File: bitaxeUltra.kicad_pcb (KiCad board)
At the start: 4 copper layers, 56.5 x 99.8 mm, 137 parts, among them J1 54-00164, J2 Conn_01x02, J3 Conn_01x05, J4 Conn_01x04, J5 TC2030-IDC, J7 Conn_01x02, J8 USB_C_Receptacle_USB2.0, J9 Conn_01x04, Q1 CSD17311Q5, Q2 CSD17311Q5, Q4 2N7002K, SW1 GT-TC029B-H025-L1N, SW2 GT-TC029B-H025-L1N, U1 25MHz, U10 DS4432U+, U11 RT9080-33GJ5, U12 ESP32-S3-WROOM-1, U14 BM1366_mode1, U2 TXB0104RGYR, U5 MCP1824T-1802E, U6 MCP1824T-0802E, U7 EMC2101, U8 INA260, U9 TPS40305, Y1 32.768kHz

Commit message: Init commit to TCH-204 Black edition with LED lights
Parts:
- removed TP23: TestPoint, TestPoint:TestPoint_Pad_D1.5mm
- added G***: LOGO, LOGO, B.Cu at (107.2, 52.8)
- added LED**: LED-RF-Controller, bitaxe:LED-RF-Controller, F.Cu at (103.1, 53.8)
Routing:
- net GND: track 148.3 -> 173.2 mm
- net /5V: track 217.6 -> 231.1 mm
- net /SDA: track 128.0 -> 126.8 mm

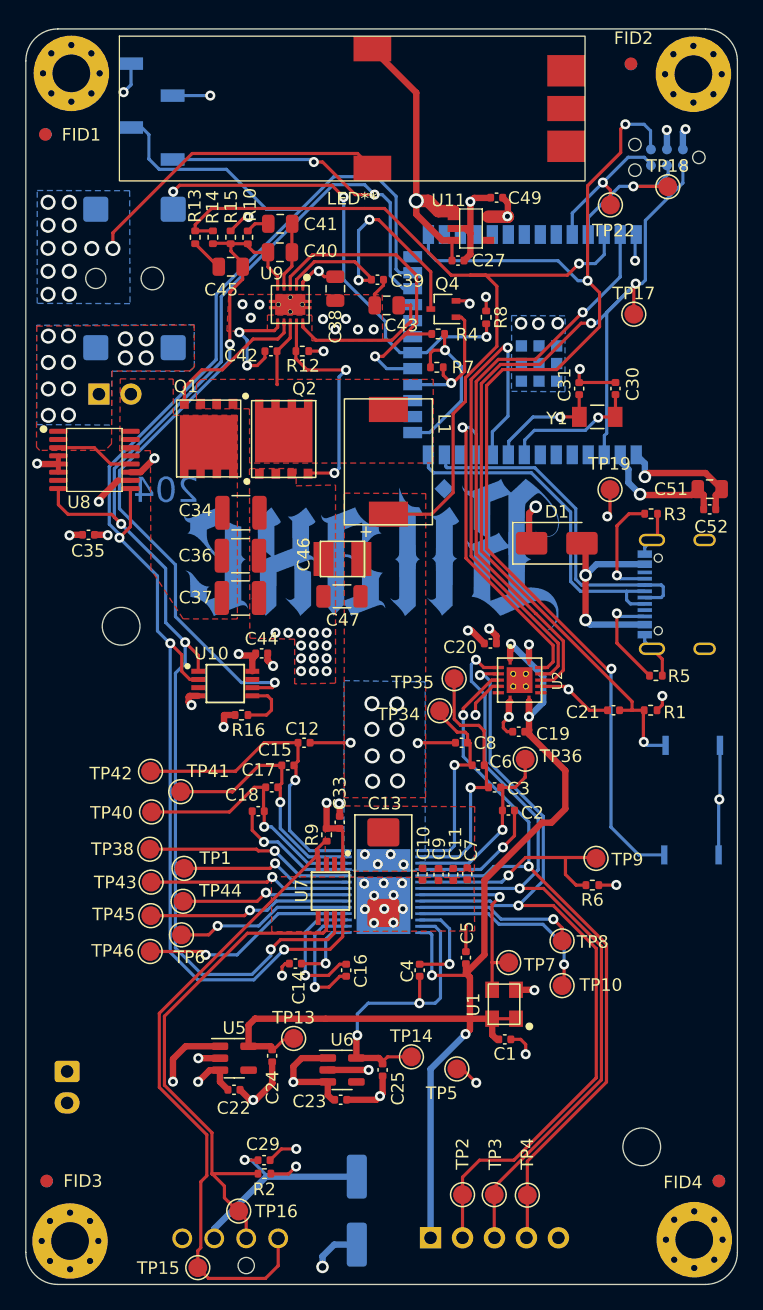
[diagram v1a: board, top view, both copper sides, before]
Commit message: Finish LED layout. Can pass to factory for prototype test
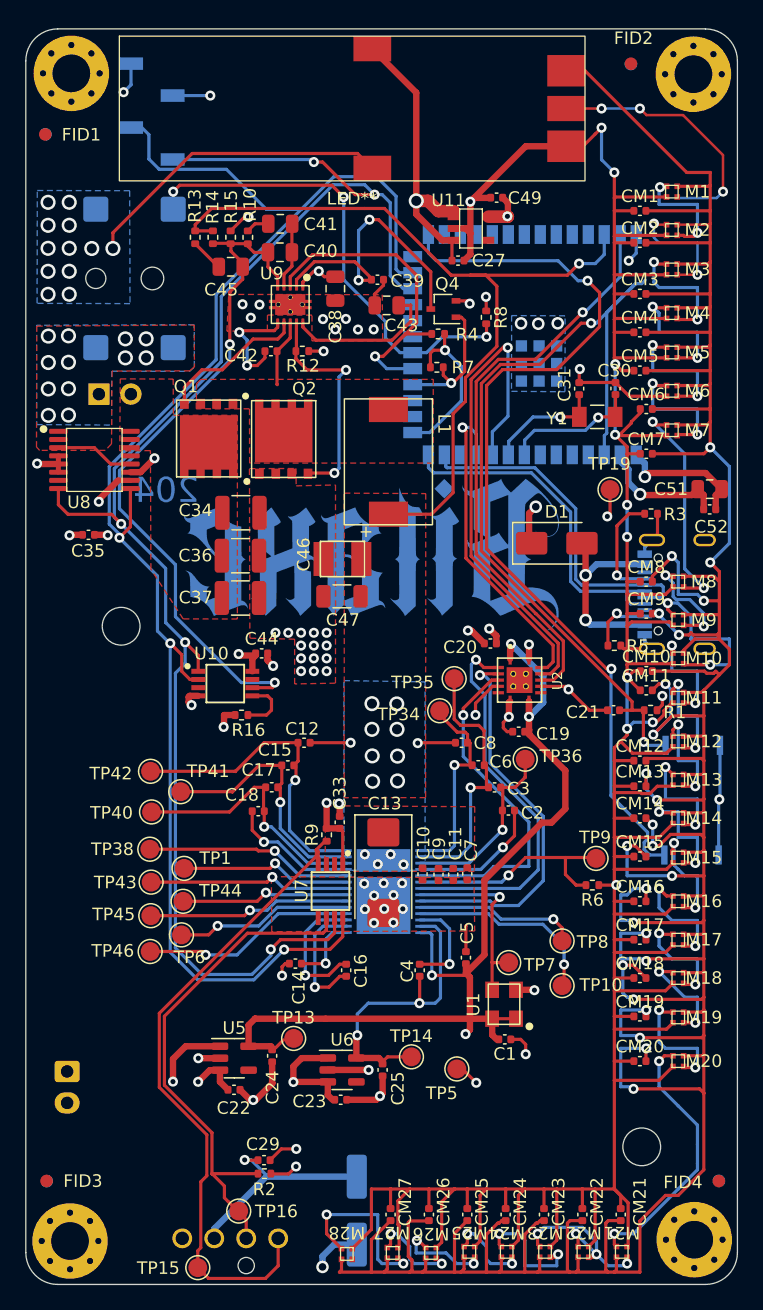
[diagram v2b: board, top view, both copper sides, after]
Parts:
- removed J3: Conn_01x05, Connector_PinHeader_2.54mm:PinHeader_1x05_P2.54mm_Vertical
- removed J5: TC2030-IDC, bitaxe:Tag-Connect_TC2030-IDC-NL_2x03_P1.27mm_Vertical
- removed TP17, TP18, TP2, TP22, TP3, TP4: TestPoint, TestPoint:TestPoint_Pad_D1.5mm
- added CM1: 0.1uF, Capacitor_SMD:C_0402_1005Metric, F.Cu at (126.0, 62.0)
- added CM10: 0.1uF, Capacitor_SMD:C_0402_1005Metric, F.Cu at (126.5, 98.6)
- added CM11: 0.1uF, Capacitor_SMD:C_0402_1005Metric, F.Cu at (126.5, 100.1)
- added CM12: 0.1uF, Capacitor_SMD:C_0402_1005Metric, F.Cu at (126.0, 105.7)
- added CM13: 0.1uF, Capacitor_SMD:C_0402_1005Metric, F.Cu at (126.0, 107.7)
- added CM14: 0.1uF, Capacitor_SMD:C_0402_1005Metric, F.Cu at (126.0, 110.2)
- added CM15: 0.1uF, Capacitor_SMD:C_0402_1005Metric, F.Cu at (126.0, 113.3)
- added CM16: 0.1uF, Capacitor_SMD:C_0402_1005Metric, F.Cu at (126.0, 116.8)
- added CM17: 0.1uF, Capacitor_SMD:C_0402_1005Metric, F.Cu at (126.0, 119.9)
- added CM18: 0.1uF, Capacitor_SMD:C_0402_1005Metric, F.Cu at (126.0, 122.9)
- added CM19: 0.1uF, Capacitor_SMD:C_0402_1005Metric, F.Cu at (126.0, 126.0)
- added CM2: 0.1uF, Capacitor_SMD:C_0402_1005Metric, F.Cu at (126.0, 64.5)
- added CM20: 0.1uF, Capacitor_SMD:C_0402_1005Metric, F.Cu at (126.0, 129.5)
- added CM21: 0.1uF, Capacitor_SMD:C_0402_1005Metric, F.Cu at (124.5, 141.7)
- added CM22: 0.1uF, Capacitor_SMD:C_0402_1005Metric, F.Cu at (121.4, 141.7)
- added CM23: 0.1uF, Capacitor_SMD:C_0402_1005Metric, F.Cu at (118.4, 141.7)
- added CM24: 0.1uF, Capacitor_SMD:C_0402_1005Metric, F.Cu at (115.3, 141.7)
- added CM25: 0.1uF, Capacitor_SMD:C_0402_1005Metric, F.Cu at (112.3, 141.7)
- added CM26: 0.1uF, Capacitor_SMD:C_0402_1005Metric, F.Cu at (109.2, 141.7)
- added CM27: 0.1uF, Capacitor_SMD:C_0402_1005Metric, F.Cu at (106.2, 141.7)
- added CM3: 0.1uF, Capacitor_SMD:C_0402_1005Metric, F.Cu at (126.0, 68.6)
- added CM4: 0.1uF, Capacitor_SMD:C_0402_1005Metric, F.Cu at (126.0, 71.6)
- added CM5: 0.1uF, Capacitor_SMD:C_0402_1005Metric, F.Cu at (126.0, 74.7)
- added CM6: 0.1uF, Capacitor_SMD:C_0402_1005Metric, F.Cu at (126.5, 77.7)
- added CM7: 0.1uF, Capacitor_SMD:C_0402_1005Metric, F.Cu at (126.5, 81.3)
- added CM8: 0.1uF, Capacitor_SMD:C_0402_1005Metric, F.Cu at (126.5, 91.4)
- added CM9: 0.1uF, Capacitor_SMD:C_0402_1005Metric, F.Cu at (126.5, 94.0)
- added M1: XL-1010RGBC, bitaxe:XL-1010RGBC, F.Cu at (128.5, 60.5)
- added M10: XL-1010RGBC, bitaxe:XL-1010RGBC, F.Cu at (129.0, 97.5)
- added M11: XL-1010RGBC, bitaxe:XL-1010RGBC, F.Cu at (129.0, 100.7)
- added M12: XL-1010RGBC, bitaxe:XL-1010RGBC, F.Cu at (129.0, 104.1)
- added M13: XL-1010RGBC, bitaxe:XL-1010RGBC, F.Cu at (129.0, 107.2)
- added M14: XL-1010RGBC, bitaxe:XL-1010RGBC, F.Cu at (129.0, 110.2)
- added M15: XL-1010RGBC, bitaxe:XL-1010RGBC, F.Cu at (129.0, 113.4)
- added M16: XL-1010RGBC, bitaxe:XL-1010RGBC, F.Cu at (129.0, 116.8)
- added M17: XL-1010RGBC, bitaxe:XL-1010RGBC, F.Cu at (129.0, 119.9)
- added M18: XL-1010RGBC, bitaxe:XL-1010RGBC, F.Cu at (129.0, 122.9)
- added M19: XL-1010RGBC, bitaxe:XL-1010RGBC, F.Cu at (129.0, 126.1)
- added M2: XL-1010RGBC, bitaxe:XL-1010RGBC, F.Cu at (128.5, 63.5)
- added M20: XL-1010RGBC, bitaxe:XL-1010RGBC, F.Cu at (129.0, 129.5)
- added M21: XL-1010RGBC, bitaxe:XL-1010RGBC, F.Cu at (124.5, 144.7)
- added M22: XL-1010RGBC, bitaxe:XL-1010RGBC, F.Cu at (121.5, 144.7)
- added M23: XL-1010RGBC, bitaxe:XL-1010RGBC, F.Cu at (118.4, 144.7)
- added M24: XL-1010RGBC, bitaxe:XL-1010RGBC, F.Cu at (115.4, 144.7)
- added M25: XL-1010RGBC, bitaxe:XL-1010RGBC, F.Cu at (112.4, 144.7)
- added M26: XL-1010RGBC, bitaxe:XL-1010RGBC, F.Cu at (109.4, 144.8)
- added M27: XL-1010RGBC, bitaxe:XL-1010RGBC, F.Cu at (106.3, 144.8)
- added M28: XL-1010RGBC, bitaxe:XL-1010RGBC, F.Cu at (102.7, 144.9)
- added M3: XL-1010RGBC, bitaxe:XL-1010RGBC, F.Cu at (128.5, 66.6)
- added M4: XL-1010RGBC, bitaxe:XL-1010RGBC, F.Cu at (128.5, 70.1)
- added M5: XL-1010RGBC, bitaxe:XL-1010RGBC, F.Cu at (128.5, 73.2)
- added M6: XL-1010RGBC, bitaxe:XL-1010RGBC, F.Cu at (128.5, 76.3)
- added M7: XL-1010RGBC, bitaxe:XL-1010RGBC, F.Cu at (128.5, 79.4)
- added M8: XL-1010RGBC, bitaxe:XL-1010RGBC, F.Cu at (129.0, 91.4)
- added M9: XL-1010RGBC, bitaxe:XL-1010RGBC, F.Cu at (129.0, 94.5)
- moved R5 4.07 mm to (124.0, 96.5)
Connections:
- LED** pad 1: (no net) -> /LED/VDD
- LED** pad 2: (no net) -> /LED/DO
- LED** pad 3: (no net) -> GND
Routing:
- net /LED/VDD: track 0.00 -> 376.4 mm, vias 0 -> 24
- net GND: track 173.2 -> 462.5 mm, vias 83 -> 91
- net /LED/DO: track 0.00 -> 146.2 mm, vias 0 -> 27
- net (no net): track 0.00 -> 143.0 mm, vias 0 -> 30
- net /BM1366/CI: track 67.5 -> 30.9 mm, vias 2 -> 1
- net /BM1366/RO: track 66.2 -> 31.1 mm, vias 2 -> 1
- net /BM1366/RST_N: track 62.1 -> 27.4 mm, vias 2 -> 1
- net /ESP32/IO0: track 92.0 -> 74.3 mm, vias 3 -> 2
- net /BM1366/1V8: track 94.1 -> 76.8 mm
- net /ESP32/EN: track 81.0 -> 68.1 mm, vias 3 -> 2
- net /ESP32/P_TX: track 12.6 -> 0.00 mm, vias 1 -> 0
- net /ESP32/P_RX: track 12.2 -> 0.00 mm, vias 1 -> 0
- net Net-(J8-CC2): track 8.33 -> 5.17 mm
- net /3V3: track 74.3 -> 72.6 mm, vias 15 -> 14

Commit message: Add Black Edition logo
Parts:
- added G***: LOGO, LOGO, B.Cu at (80.8, 111.3)

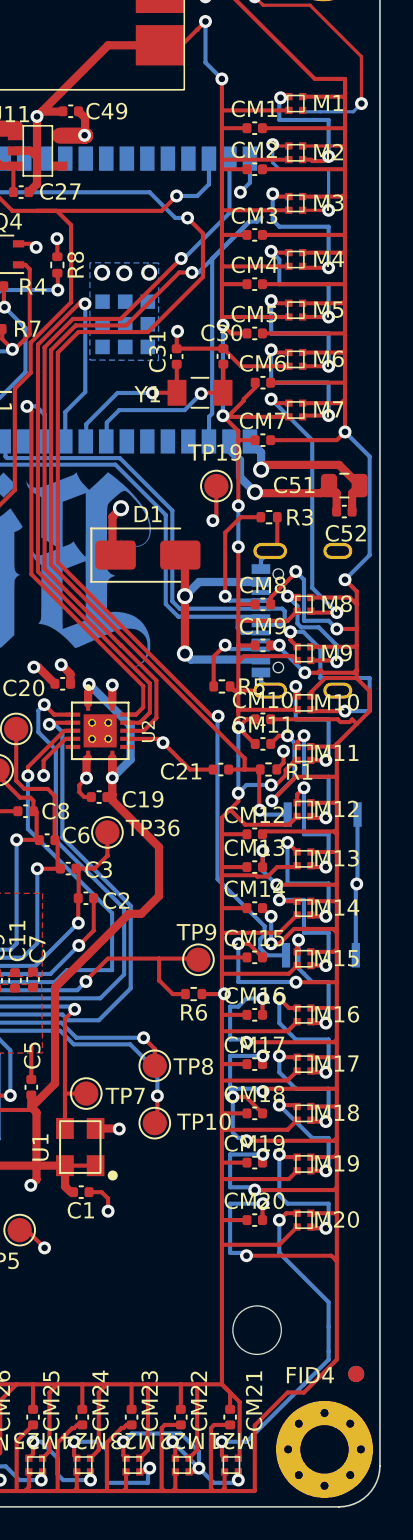
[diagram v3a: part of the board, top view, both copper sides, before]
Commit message: Fix Led wiring issue
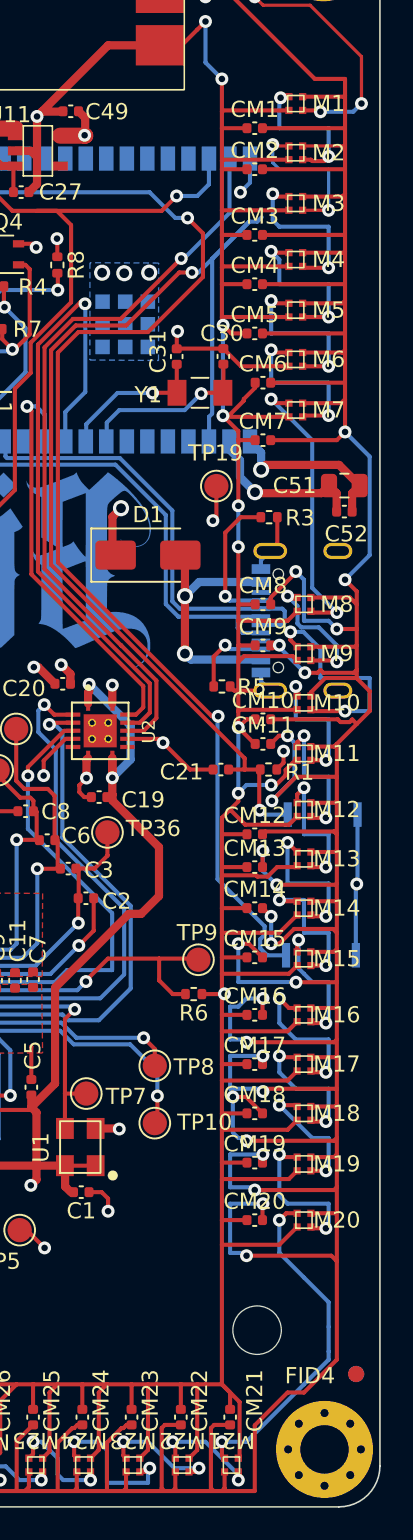
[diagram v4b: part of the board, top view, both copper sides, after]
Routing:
- net (no net): track 143.0 -> 142.0 mm
- net /LED/DO: track 146.2 -> 146.3 mm, vias 27 -> 28
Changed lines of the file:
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@@
   (segment (start 130.556 121.412) (end 130.556 123.2731) (width 0.254) (layer "B.Cu") (net 0))
   (segment (start 130.556 134.62) (end 130.556 136.144) (width 0.254) (layer "B.Cu") (net 0))
+  (segment (start 122.535253 144.887253) (end 121.011253 144.887253) (width 0.254) (layer "B.Cu") (net 0))
   (segment (start 128.696238 112.205954) (end 128.696238 113.964238) (width 0.254) (layer "B.Cu") (net 0))
   (segment (start 130.556 129.8771) (end 130.3851 130.048) (width 0.254) (layer "B.Cu") (net 0))
@@
   (segment (start 128.524 121.412) (end 130.556 121.412) (width 0.254) (layer "B.Cu") (net 0))
   (segment (start 127.508 125.476) (end 127.508 128.016) (width 0.254) (layer "B.Cu") (net 0))
-  (segment (start 122.535253 144.887253) (end 122.535253 143.871253) (width 0.254) (layer "B.Cu") (net 0))
   (segment (start 113.792 145.288) (end 113.792 144.272) (width 0.254) (layer "B.Cu") (net 0))
   (segment (start 114.1291 145.6251) (end 113.792 145.288) (width 0.254) (layer "B.Cu") (net 0))
-  (segment (start 124.7971 145.796) (end 124.968 145.6251) (width 0.254) (layer "B.Cu") (net 0))
-  (segment (start 122.535253 143.871253) (end 121.412 142.748) (width 0.254) (layer "B.Cu") (net 0))
   (segment (start 129.54 114.808) (end 130.556 114.808) (width 0.254) (layer "B.Cu") (net 0))
   (segment (start 130.556 128.524) (end 130.556 129.8771) (width 0.254) (layer "B.Cu") (net 0))
@@
   (segment (start 129.54 124.46) (end 130.556 124.46) (width 0.254) (layer "B.Cu") (net 0))
   (segment (start 116.84 145.796) (end 116.84 143.764) (width 0.254) (layer "B.Cu") (net 0))
-  (segment (start 121.412 142.748) (end 118.364 142.748) (width 0.254) (layer "B.Cu") (net 0))
   (segment (start 115.824 145.6251) (end 114.1291 145.6251) (width 0.254) (layer "B.Cu") (net 0))
-  (segment (start 123.444 145.796) (end 124.7971 145.796) (width 0.254) (layer "B.Cu") (net 0))
   (segment (start 112.776 143.256) (end 112.268 143.256) (width 0.254) (layer "B.Cu") (net 0))
-  (segment (start 118.364 142.748) (end 117.856 143.256) (width 0.254) (layer "B.Cu") (net 0))
   (segment (start 130.556 136.144) (end 130.556 137.668) (width 0.254) (layer "B.Cu") (net 0))
+  (segment (start 120.904 143.256) (end 122.936 143.256) (width 0.254) (layer "B.Cu") (net 0))
   (segment (start 130.556 126.3211) (end 130.3851 126.492) (width 0.254) (layer "B.Cu") (net 0))
+  (segment (start 122.936 143.256) (end 124.968 145.288) (width 0.254) (layer "B.Cu") (net 0))
+  (segment (start 124.968 145.288) (end 124.968 145.6251) (width 0.254) (layer "B.Cu") (net 0))
   (segment (start 129.032 111.76) (end 130.556 111.76) (width 0.254) (layer "B.Cu") (net 0))
   (segment (start 130.556 114.808) (end 130.556 117.1771) (width 0.254) (layer "B.Cu") (net 0))
   (segment (start 128.016 120.904) (end 128.524 121.412) (width 0.254) (layer "B.Cu") (net 0))
   (segment (start 128.524 118.364) (end 130.556 118.364) (width 0.254) (layer "B.Cu") (net 0))
+  (segment (start 121.011253 144.887253) (end 119.38 143.256) (width 0.254) (layer "B.Cu") (net 0))
   (segment (start 105.156 141.732) (end 101.092 141.732) (width 0.254) (layer "B.Cu") (net 0))
   (segment (start 130.556 137.668) (end 130.556 138.176) (width 0.254) (layer "B.Cu") (net 0))
@@
   (segment (start 128.016 108.712) (end 130.556 108.712) (width 0.254) (layer "B.Cu") (net 0))
   (segment (start 128.016 117.856) (end 128.524 118.364) (width 0.254) (layer "B.Cu") (net 0))
+  (segment (start 119.38 143.256) (end 117.856 143.256) (width 0.254) (layer "B.Cu") (net 0))
   (segment (start 129.032 139.7) (end 125.476 143.256) (width 0.254) (layer "B.Cu") (net 0))
   (segment (start 130.556 124.46) (end 130.556 126.3211) (width 0.254) (layer "B.Cu") (net 0))
-  (segment (start 120.904 143.256) (end 123.444 145.796) (width 0.254) (layer "B.Cu") (net 0))
   (segment (start 127.508 122.428) (end 129.54 124.46) (width 0.254) (layer "B.Cu") (net 0))
   (segment (start 127.508 120.396) (end 128.016 120.904) (width 0.254) (layer "B.Cu") (net 0))
@@
   (segment (start 131.572 80.772) (end 133.096 82.296) (width 0.254) (layer "B.Cu") (net 94))
   (segment (start 128.607 97.111) (end 128.607 96.603) (width 0.254) (layer "F.Cu") (net 95))
+  (segment (start 128.949 60.877) (end 129.965 60.877) (width 0.254) (layer "F.Cu") (net 95))
   (segment (start 128.607 99.993) (end 128.607 100.242) (width 0.254) (layer "F.Cu") (net 95))
   (segment (start 129.54 104.648) (end 129.457 104.565) (width 0.254) (layer "F.Cu") (net 95))
@@
   (segment (start 130.556 79.756) (end 129.032 79.756) (width 0.254) (layer "F.Cu") (net 95))
   (segment (start 128.607 96.603) (end 128.524 96.52) (width 0.254) (layer "F.Cu") (net 95))
+  (segment (start 129.965 60.877) (end 130.048 60.96) (width 0.254) (layer "F.Cu") (net 95))
   (segment (start 127.083 69.679) (end 127 69.596) (width 0.254) (layer "F.Cu") (net 95))
   (segment (start 127.652201 60.027) (end 127.584401 60.0948) (width 0.254) (layer "F.Cu") (net 95))
@@
   (via (at 127 75.692) (size 0.8) (drill 0.4) (layers "F.Cu" "B.Cu") (net 95))
   (via (at 130.556 76.708) (size 0.8) (drill 0.4) (layers "F.Cu" "B.Cu") (net 95))
+  (via (at 130.048 60.96) (size 0.8) (drill 0.4) (layers "F.Cu" "B.Cu") (net 95))
   (via (at 128.524 96.52) (size 0.8) (drill 0.4) (layers "F.Cu" "B.Cu") (net 95))
   (via (at 132.588 60.452) (size 0.8) (drill 0.4) (layers "F.Cu" "B.Cu") (net 95))
@@
   (via (at 130.3851 101.092) (size 0.8) (drill 0.4) (layers "F.Cu" "B.Cu") (net 95))
   (via (at 130.556 79.756) (size 0.8) (drill 0.4) (layers "F.Cu" "B.Cu") (net 95))
+  (segment (start 132.08 60.96) (end 132.588 60.452) (width 0.254) (layer "B.Cu") (net 95))
   (segment (start 122.936 53.848) (end 125.984 53.848) (width 0.2) (layer "B.Cu") (net 95))
   (segment (start 130.556 71.628) (end 130.556 73.66) (width 0.254) (layer "B.Cu") (net 95))
@@
   (segment (start 127.0983 64.1063) (end 127.508 64.516) (width 0.2) (layer "B.Cu") (net 95))
   (segment (start 127.508 71.628) (end 130.556 71.628) (width 0.254) (layer "B.Cu") (net 95))
-  (segment (start 132.08 60.96) (end 130.048 60.96) (width 0.2) (layer "B.Cu") (net 95))
   (segment (start 130.556 74.676) (end 130.556 76.708) (width 0.254) (layer "B.Cu") (net 95))
   (segment (start 130.556 105.664) (end 130.556 107.5251) (width 0.254) (layer "B.Cu") (net 95))
+  (segment (start 127.508 61.976) (end 130.556 61.976) (width 0.254) (layer "B.Cu") (net 95))
   (segment (start 127.508 68.072) (end 130.556 68.072) (width 0.254) (layer "B.Cu") (net 95))
   (segment (start 128.016 90.932) (end 128.6256 91.5416) (width 0.254) (layer "B.Cu") (net 95))
+  (segment (start 127.508 60.171201) (end 127.508 61.976) (width 0.254) (layer "B.Cu") (net 95))
   (segment (start 130.556 64.516) (end 130.556 67.056) (width 0.2) (layer "B.Cu") (net 95))
   (segment (start 130.048 94.200563) (end 130.048 96.012) (width 0.254) (layer "B.Cu") (net 95))
@@
   (segment (start 127 74.676) (end 130.556 74.676) (width 0.254) (layer "B.Cu") (net 95))
   (segment (start 127.0983 66.04) (end 127.0983 67.6623) (width 0.254) (layer "B.Cu") (net 95))
+  (segment (start 130.556 61.976) (end 130.556 63.7269) (width 0.254) (layer "B.Cu") (net 95))
   (segment (start 130.556 100.9211) (end 130.3851 101.092) (width 0.254) (layer "B.Cu") (net 95))
   (segment (start 129.032 102.108) (end 130.556 102.108) (width 0.254) (layer "B.Cu") (net 95))
-  (segment (start 132.588 60.452) (end 132.08 60.96) (width 0.2) (layer "B.Cu") (net 95))
-  (segment (start 127.508 60.171201) (end 127.508 61.468) (width 0.254) (layer "B.Cu") (net 95))
-  (segment (start 130.556 61.468) (end 130.556 63.7269) (width 0.254) (layer "B.Cu") (net 95))
   (segment (start 133.096 98.044) (end 131.572 98.044) (width 0.254) (layer "B.Cu") (net 95))
   (segment (start 128.196055 93.144055) (end 128.991492 93.144055) (width 0.254) (layer "B.Cu") (net 95))
@@
   (segment (start 128.524 96.52) (end 128.524 98.552) (width 0.254) (layer "B.Cu") (net 95))
   (segment (start 128.6256 92.624336) (end 128.863664 92.8624) (width 0.254) (layer "B.Cu") (net 95))
-  (segment (start 127.508 61.468) (end 130.556 61.468) (width 0.254) (layer "B.Cu") (net 95))
   (segment (start 127 75.692) (end 127 77.724) (width 0.254) (layer "B.Cu") (net 95))
   (segment (start 129.54 90.424) (end 131.064 91.948) (width 0.254) (layer "B.Cu") (net 95))
@@
   (segment (start 127.508 64.516) (end 130.556 64.516) (width 0.2) (layer "B.Cu") (net 95))
   (segment (start 129.032 102.7869) (end 129.032 105.664) (width 0.254) (layer "B.Cu") (net 95))
+  (segment (start 127.584401 60.0948) (end 127.508 60.171201) (width 0.254) (layer "B.Cu") (net 95))
   (segment (start 130.556 104.4771) (end 130.3851 104.648) (width 0.254) (layer "B.Cu") (net 95))
   (segment (start 127 77.724) (end 130.556 77.724) (width 0.254) (layer "B.Cu") (net 95))
   (segment (start 130.556 107.5251) (end 130.3851 107.696) (width 0.254) (layer "B.Cu") (net 95))
   (segment (start 129.54 81.28) (end 129.54 90.424) (width 0.254) (layer "B.Cu") (net 95))
-  (segment (start 127.584401 60.0948) (end 127.508 60.171201) (width 0.254) (layer "B.Cu") (net 95))
   (segment (start 133.096 96.012) (end 133.096 98.044) (width 0.254) (layer "B.Cu") (net 95))
-  (segment (start 130.048 60.96) (end 129.032 60.96) (width 0.2) (layer "B.Cu") (net 95))
   (segment (start 127.0983 67.6623) (end 127.508 68.072) (width 0.254) (layer "B.Cu") (net 95))
+  (segment (start 130.048 60.96) (end 132.08 60.96) (width 0.254) (layer "B.Cu") (net 95))
   (segment (start 130.556 98.552) (end 130.556 100.9211) (width 0.254) (layer "B.Cu") (net 95))
   (segment (start 129.032 99.568) (end 129.032 102.108) (width 0.254) (layer "B.Cu") (net 95))
